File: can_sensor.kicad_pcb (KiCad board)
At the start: 2 copper layers, 53.3 x 25.4 mm, 54 parts, among them P1 IO1, P2 IO2, P4 CONN_01X03, P5 USB, P6 CAN_IN, P7 CAN_OUT, P8 TERM, Q1 Q_PMOS_GSD, SW1 RESET, SW2 BOOT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

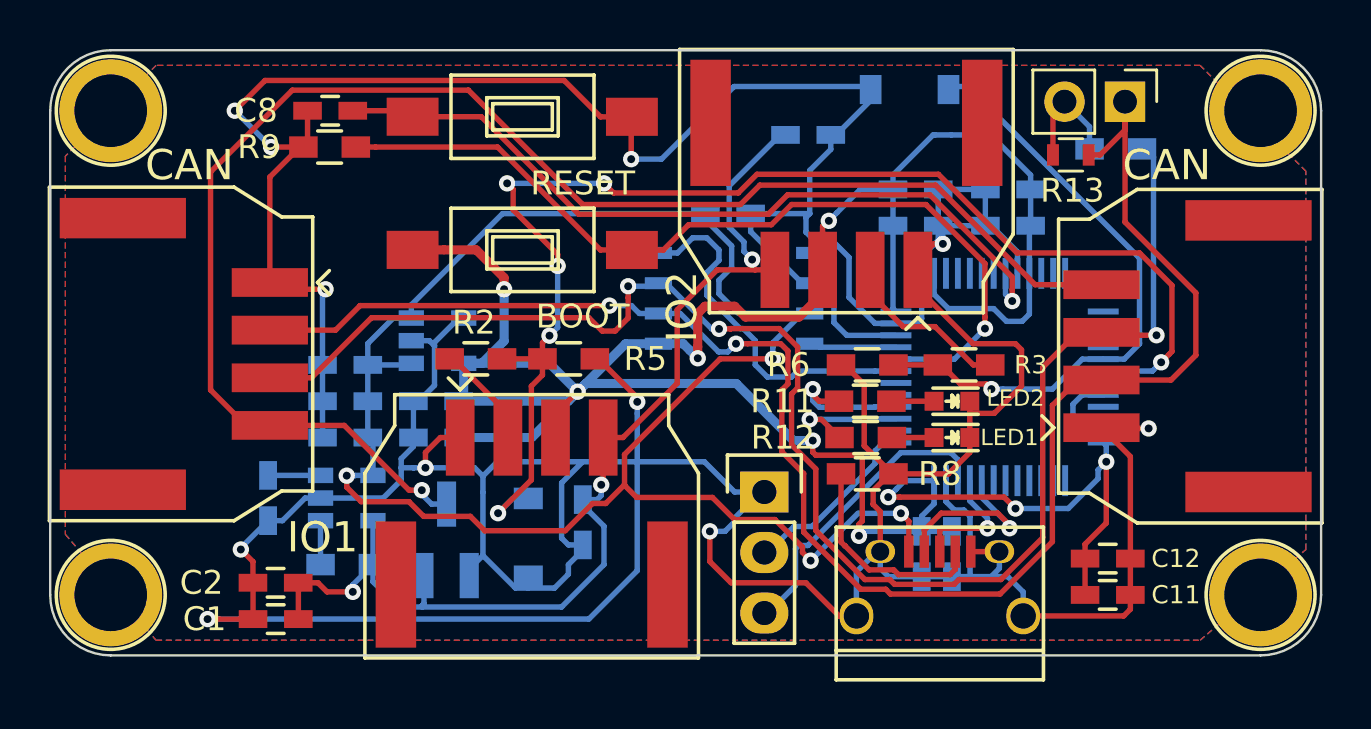
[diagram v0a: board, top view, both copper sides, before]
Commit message: finished adding footprints & started routing
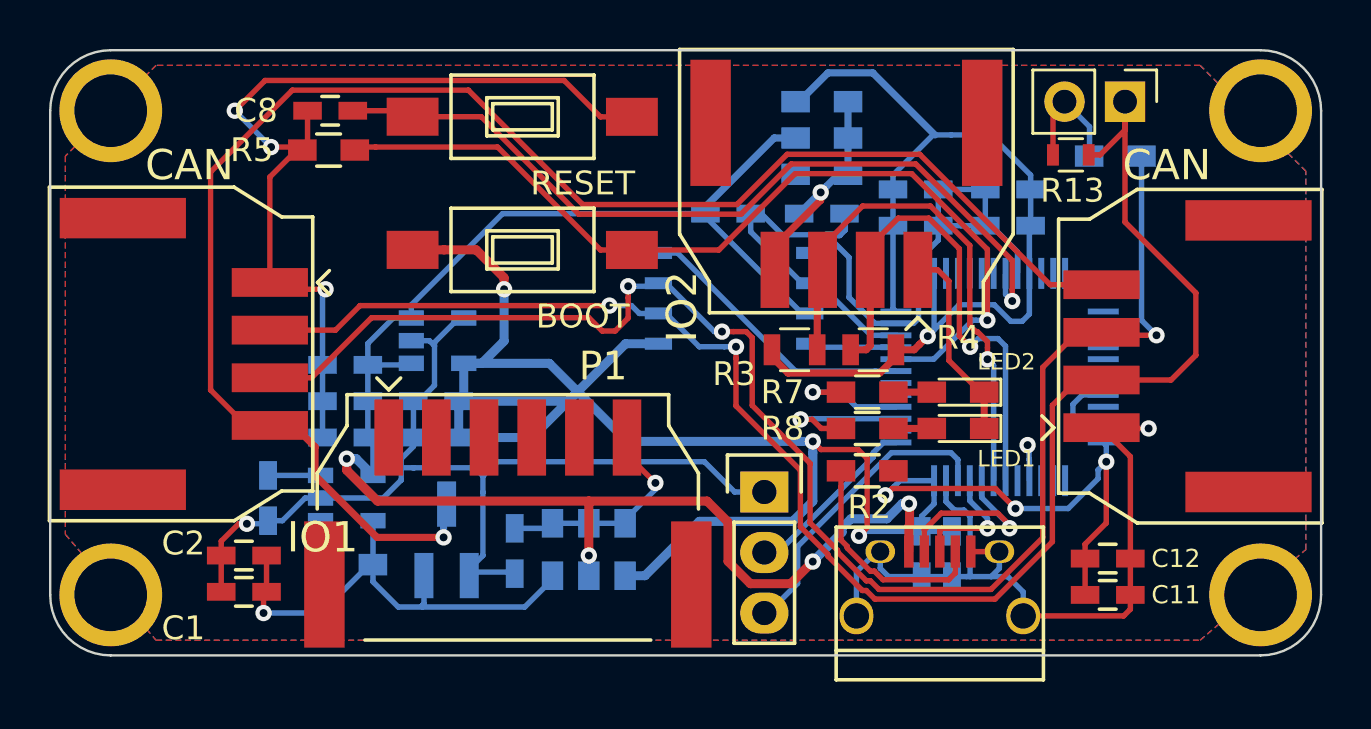
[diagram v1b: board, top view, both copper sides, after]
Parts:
- removed D8: LED1, LEDs:LED_0603
- removed D9: LED2, LEDs:LED_0603
- removed G***: LOGO, User_Random:TwoFacedMan
- removed R10, R11, R12: 120R, Resistors_SMD:R_0603_HandSoldering
- removed R9: 100K, Resistors_SMD:R_0603_HandSoldering
- removed REF** (x4): 1pin, Connect:1pin
- added J1: TEST_1P, Mounting_Holes:MountingHole_3.2mm_M3_ISO7380_Pad, F.Cu at (111.8, 117.5)
- added J2: TEST_1P, Mounting_Holes:MountingHole_3.2mm_M3_ISO7380_Pad, F.Cu at (111.8, 97.2)
- added J3: TEST_1P, Mounting_Holes:MountingHole_3.2mm_M3_ISO7380_Pad, F.Cu at (160.0, 97.2)
- added J4: TEST_1P, Mounting_Holes:MountingHole_3.2mm_M3_ISO7380_Pad, F.Cu at (160.0, 117.5)
- added JP1: Vin, Resistors_SMD:R_0603_HandSoldering, B.Cu at (130.3, 115.6)
- added JP2: Vin, Resistors_SMD:R_0603_HandSoldering, B.Cu at (141.6, 99.8)
- added JP3: 3V, Resistors_SMD:R_0603_HandSoldering, B.Cu at (131.8, 115.6)
- added JP4: 3V, Resistors_SMD:R_0603_HandSoldering, B.Cu at (141.6, 98.3)
- added JP5: 5V, Resistors_SMD:R_0603_HandSoldering, B.Cu at (133.3, 115.6)
- added JP6: 5V, Resistors_SMD:R_0603_HandSoldering, B.Cu at (141.6, 96.8)
- added R4: 4K7, Resistors_SMD:R_0805, F.Cu at (143.8, 107.2)
- added R7: 120R, Resistors_SMD:R_0603_HandSoldering, F.Cu at (143.5, 109.0)
- D1: value D_Zener_Small -> LED1; footprint Diodes_SMD:SOD-123 -> LEDs:LED_0603_HandSoldering; moved to F.Cu
- D2: value D_Zener_Small -> LED2; footprint Diodes_SMD:SOD-123 -> LEDs:LED_0603_HandSoldering; moved to F.Cu
- P1: value IO1 -> SPI; footprint User_Connectors:Molex-duraClick-4conn -> Supermileage:Molex-duraClick-6conn
- P2: value IO2 -> I2C
- P4: value CONN_01X03 -> STLink
- R2, R5: value R -> 100K
- R3: value R -> 4K7; footprint Resistors_SMD:R_0603_HandSoldering -> Resistors_SMD:R_0805
- R6: value R -> 120R; moved to B.Cu
- R8: value 100K -> 120R
- moved C19 21.4 mm to (128.7, 115.6), turned to 270 degrees
- moved D1 19.0 mm to (147.3, 109.0), turned to 180 degrees
- moved R2 17.1 mm to (143.5, 112.3), turned to 0 degrees
- moved C20 16.4 mm to (141.6, 101.5), turned to 0 degrees
- moved D2 14.4 mm to (147.3, 110.5)
- moved R6 13.6 mm to (153.9, 99.1)
- moved R5 13.4 mm to (120.9, 98.8), turned to 180 degrees
- moved R3 7.14 mm to (140.5, 107.2)
- moved R8 1.91 mm to (143.5, 110.5), turned to 180 degrees
- moved C1 1.76 mm to (117.3, 117.3)
- moved C2 1.75 mm to (117.3, 115.8)
- moved P1 1.00 mm to (128.4, 110.9)
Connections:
- C19 pad 1: VDD -> Net-(C19-Pad1)
- C20 pad 1: VDD -> Net-(C20-Pad1)
- D1 pad 1: /io1 -> GND
- D1 pad 2: GND -> Net-(D1-Pad2)
- D2 pad 1: /io2 -> GND
- D2 pad 2: GND -> Net-(D2-Pad2)
- P1 pad 2: Net-(P1-Pad2) -> /SPI_MISO
- P1 pad 3: +3V3 -> /SPI_MOSI
- P1 pad 4: VDD -> /SPI_SCK
- P2 pad 2: Net-(P2-Pad2) -> /I2C_SDA
- P2 pad 3: +3V3 -> /I2C_SCL
- P2 pad 4: VDD -> Net-(C20-Pad1)
- R2 pad 1: /io1 -> Net-(P5-Pad4)
- R2 pad 2: Net-(P1-Pad2) -> GND
- R3 pad 1: /io2 -> +3V3
- R3 pad 2: Net-(P2-Pad2) -> /I2C_SCL
- R5 pad 1: /io1 -> Net-(R5-Pad1)
- R6 pad 1: /io2 -> /CAN_H
- R6 pad 2: GND -> Net-(P8-Pad2)
- R8 pad 1: Net-(P5-Pad4) -> Net-(D2-Pad2)
- R8 pad 2: GND -> /LED2
- SW2 pad 2: Net-(R9-Pad1) -> Net-(R5-Pad1)
- U3 pad 17: /io2 -> Net-(U3-Pad17)
- U3 pad 25: Net-(U3-Pad25) -> /SPI_NSS
- U3 pad 26: Net-(U3-Pad26) -> /SPI_SCK
- U3 pad 27: Net-(U3-Pad27) -> /SPI_MISO
- U3 pad 28: Net-(U3-Pad28) -> /SPI_MOSI
- U3 pad 30: Net-(U3-Pad30) -> /I2C_SDA
- U3 pad 31: Net-(U3-Pad31) -> /I2C_SCL
- U3 pad 44: Net-(R9-Pad1) -> Net-(R5-Pad1)
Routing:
- net GND: track 250.9 -> 157.6 mm, vias 11 -> 5
- net /io1: track 55.5 -> 0.00 mm, vias 6 -> 0
- net Net-(R5-Pad1): track 0.00 -> 38.4 mm, vias 0 -> 1
- net Net-(R9-Pad1): track 37.0 -> 0.00 mm, vias 1 -> 0
- net /io2: track 26.2 -> 0.00 mm, vias 1 -> 0
- net VDD: track 45.8 -> 20.7 mm, vias 3 -> 1
- net /I2C_SCL: track 0.00 -> 23.3 mm, vias 0 -> 1
- net /I2C_SDA: track 0.00 -> 22.5 mm, vias 0 -> 1
- net +3V3: track 119.2 -> 130.5 mm, vias 9 -> 7
- net Net-(C20-Pad1): track 0.00 -> 10.2 mm, vias 0 -> 1
- net Net-(C19-Pad1): track 0.00 -> 9.34 mm, vias 0 -> 1
- net Net-(P2-Pad2): track 7.27 -> 0.00 mm
- net Net-(P1-Pad2): track 4.40 -> 0.00 mm
- net +5V: track 75.1 -> 71.1 mm
- net /Vin: track 64.0 -> 67.6 mm
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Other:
- board text added: "3.3V"
- board text added: "5V"
- board text added: "Sam Ellicott - Fall 2017"
- board text added: "SerialBreakout"
- board text added: "Vin"
- board text removed: "CanSensor 2.0"
- board text removed: "IN-[R2]-+-OUT | [R5] | GND"
- board text removed: "R2 (R3) and R5 (R6) attenuate input voltage"
- board text removed: "Sam Ellicott - Summer 2017"

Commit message: Changed title and added pdf
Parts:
- R3, R4, R7, R8: moved to B.Cu
- moved R3 15.4 mm to (152.7, 116.6), turned to 180 degrees
- moved R4 11.6 mm to (152.6, 114.7)
- moved D2 7.10 mm to (141.0, 107.3)
- moved D1 2.87 mm to (145.0, 107.3)
- moved R8 2.23 mm to (141.3, 110.3), turned to 0 degrees
- moved R7 2.22 mm to (141.3, 108.9), turned to 0 degrees
- moved C15 0.13 mm to (145.7, 115.8)
- moved C16 0.09 mm to (147.0, 115.8)
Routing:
- net VDD: track 20.7 -> 52.4 mm, vias 1 -> 3
- net /SPI_MISO: track 0.00 -> 29.9 mm, vias 0 -> 1
- net /SPI_SCK: track 0.00 -> 26.2 mm, vias 0 -> 1
- net /SPI_MOSI: track 1.52 -> 26.6 mm
- net /SPI_NSS: track 0.00 -> 25.1 mm, vias 0 -> 1
- net GND: track 157.6 -> 179.3 mm, vias 5 -> 9
- net /CAN_H: track 65.2 -> 50.8 mm
- net /CAN_L: track 69.9 -> 56.8 mm
- net Net-(D1-Pad2): track 1.61 -> 13.9 mm, vias 0 -> 1
- net +3V3: track 130.5 -> 139.0 mm
- net Net-(D2-Pad2): track 1.61 -> 8.89 mm, vias 0 -> 1
- net +5V: track 71.1 -> 75.1 mm
- net /Vin: track 67.6 -> 71.2 mm, vias 1 -> 3
- net /LED2: track 5.86 -> 2.46 mm, vias 1 -> 0
- net /USB_DM: track 7.59 -> 10.8 mm
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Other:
- board text added: "I2C"
- board text added: "I2C 1: GND 2: SDA 3: SCL 4: PWR"
- board text added: "SPI"
- board text added: "SPI 1: GND 2: MISO 3: MOSI 4: SCK 5: SS 6: PWR"
- board text added: "Serial Breakout V1.0"
- board text added: "Short one of the VDD, 5V, or 3.3V jumpers for each output"
- board text removed: "IO 1: GND 2: IO 3: 3.3v 4: Vin"
- board text removed: "IO1"
- board text removed: "IO2"
- board text removed: "SerialBreakout"
